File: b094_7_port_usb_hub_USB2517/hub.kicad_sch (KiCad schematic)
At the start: 33 parts, among them IC1 USB2517-JZX, U1 MIC2019YM6, U2 MIC2019YM6, U3 MIC2019YM6, U4 MIC2019YM6, U5 MIC2019YM6, U6 MIC2019YM6, U7 MIC2019YM6, Y1 Crystal_GND24_Small

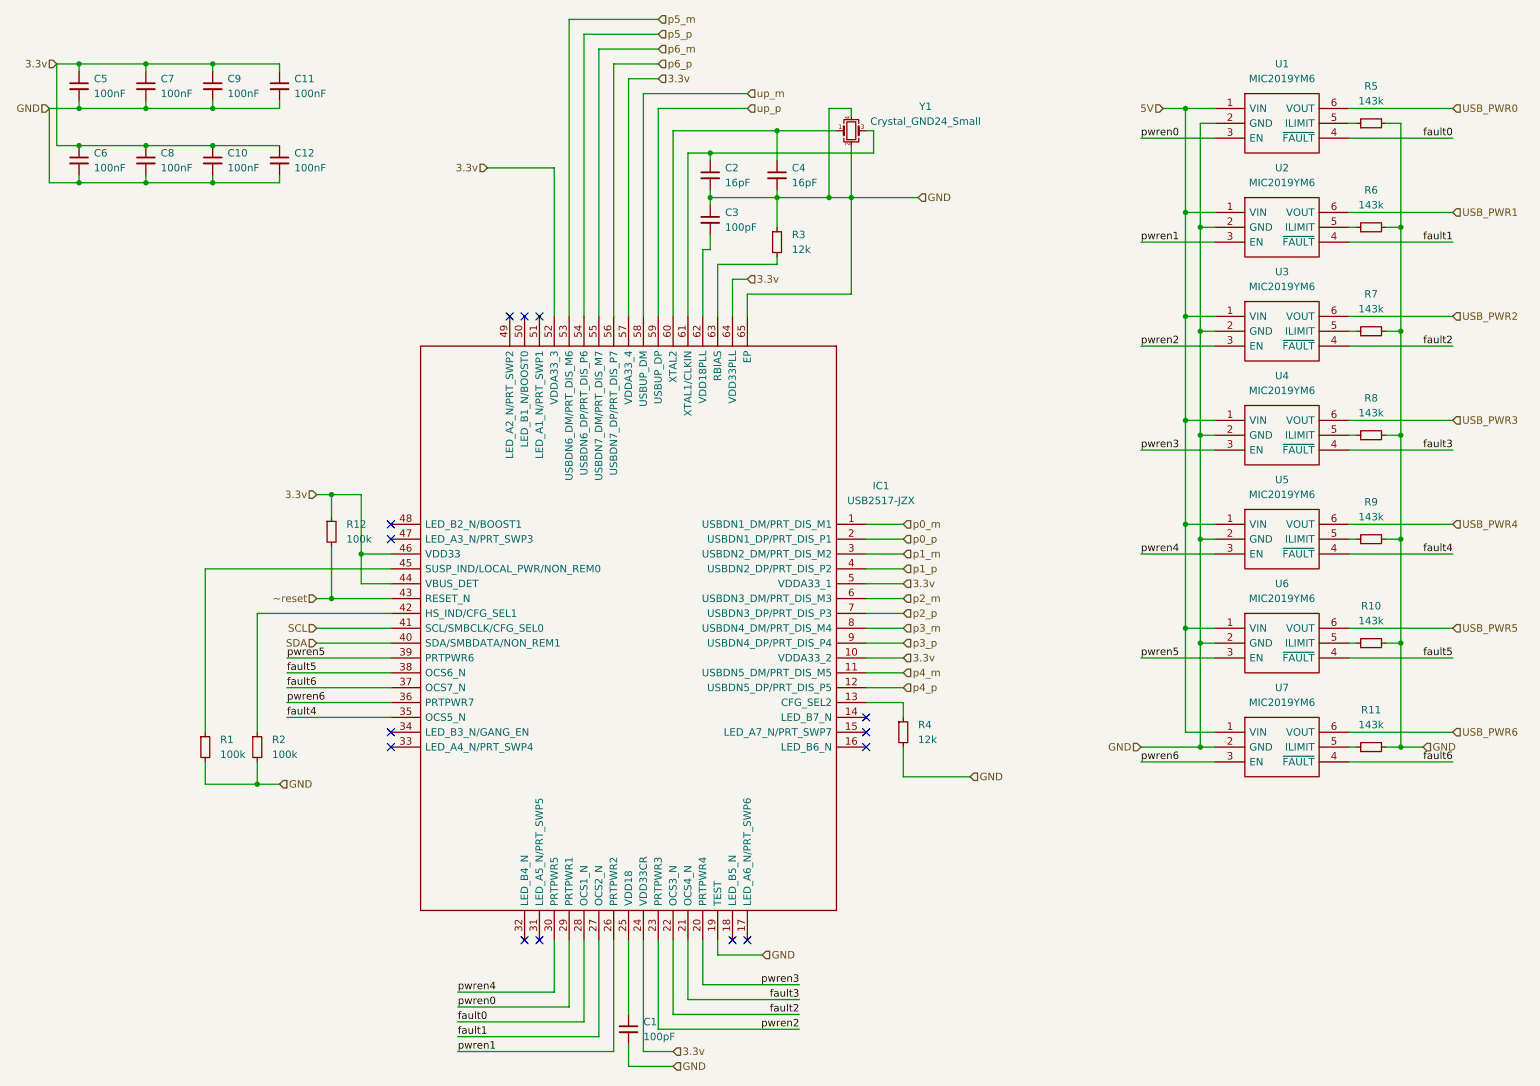
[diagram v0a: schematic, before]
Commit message: added strapping and quartz resistors
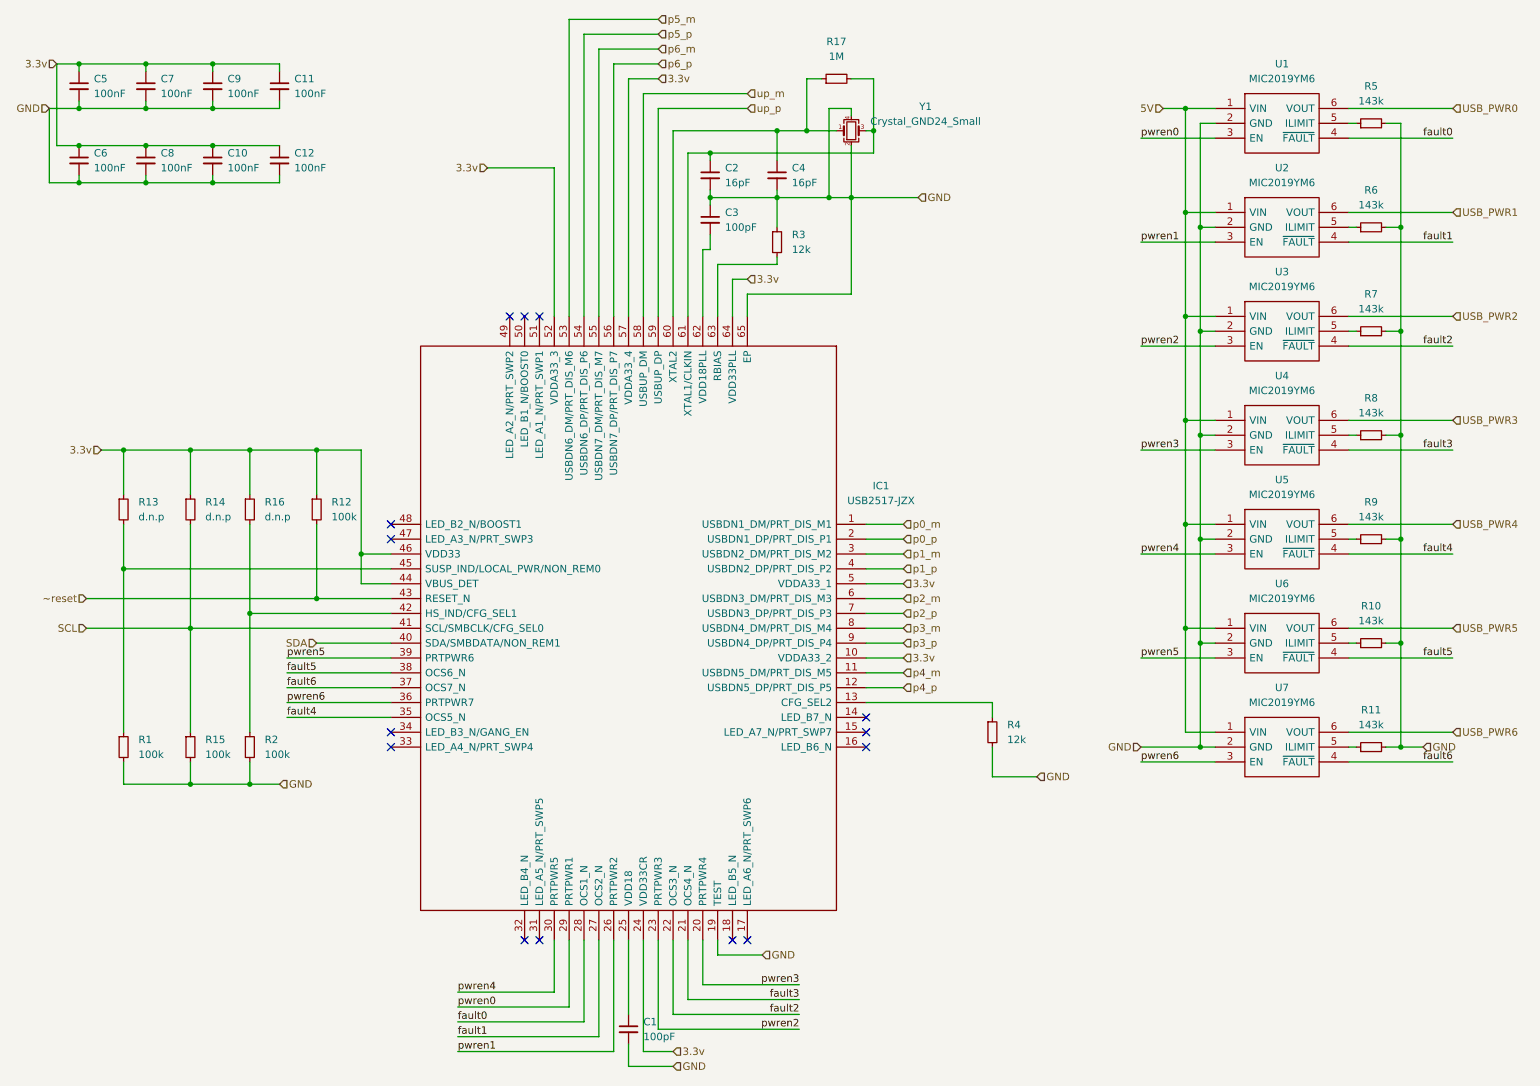
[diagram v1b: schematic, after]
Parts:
- added R13, R14, R16: d.n.p, Capacitor_SMD:C_0603_1608Metric, symbol Device:R_Small
- added R15: 100k, Capacitor_SMD:C_0603_1608Metric, symbol Device:R_Small
- added R17: 1M, Capacitor_SMD:C_0603_1608Metric, symbol Device:R_Small
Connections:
- net 3.3v: now also R13.1, R14.1, R16.1
- net GND: now also R15.2
- net SCL: now also R14.2, R15.1
- net at IC1.42 (HS_IND/CFG_SEL1), R2.1: now also R16.2
- net at C4.1, IC1.60 (XTAL2), Y1.1: now also R17.1
- net at C2.1, IC1.61 (XTAL1/CLKIN), Y1.3: now also R17.2
- net at IC1.45 (SUSP_IND/LOCAL_PWR/NON_REM0), R1.1: now also R13.2
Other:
- moved on the sheet: R1, R12, R2, R4
